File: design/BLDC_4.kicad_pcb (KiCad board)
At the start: 4 copper layers, 39.9 x 97.5 mm, 120 parts, among them J1 Conn_01x02_Pin, J101 Conn_02x16_Odd_Even, J2 Conn_01x02_Pin, J3 Conn_01x02_Pin, J4 Conn_01x02_Pin, J803 USB_C_Receptacle_USB2.0_16P, Q1 IRFS7530, Q2 IRFS7530, Q3 IRFS7530, Q4 IRFS7530, Q5 IRFS7530, Q6 IRFS7530, U1 STM32F40X_LQFP64, U2 TC2117, U3 DRV8302, U401 SN65HVD232, X2 8MHz 10ppm

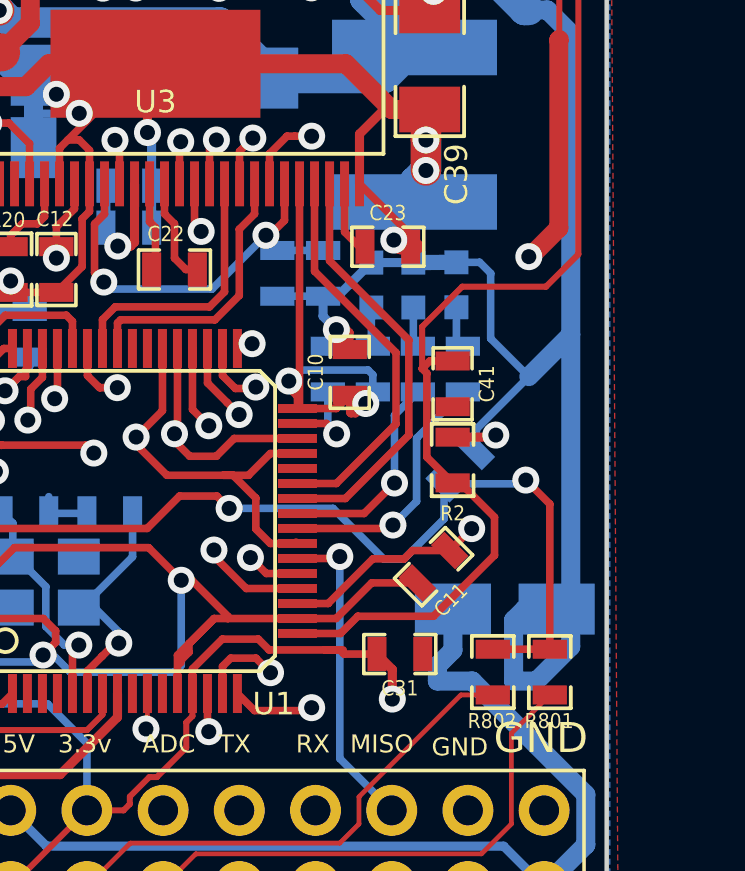
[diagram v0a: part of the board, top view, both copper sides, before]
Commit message: moved LEDs to front
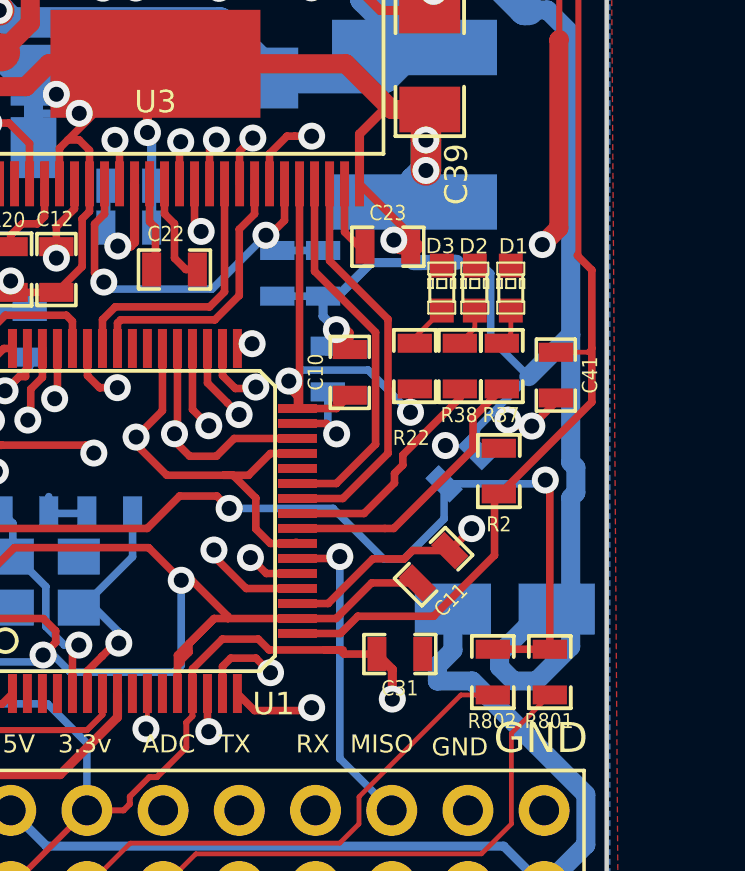
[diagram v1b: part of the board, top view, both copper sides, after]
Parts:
- D1, D2, D3, R22, R37, R38: moved to F.Cu
- moved C41 3.45 mm to (115.2, 126.2)
- moved D3 2.35 mm to (111.4, 123.3)
- moved D2 2.05 mm to (112.5, 123.3)
- moved D1 1.82 mm to (113.7, 123.3)
- moved R2 1.58 mm to (113.3, 129.4)
- moved R22 1.40 mm to (110.5, 125.9)
- moved R38 1.40 mm to (112.0, 125.9)
- moved R37 1.30 mm to (113.4, 125.9)
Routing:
- net /MCU/ADC_TEMP: track 58.0 -> 54.8 mm
- net GND: track 299.6 -> 300.5 mm, vias 29 -> 31
- net /MCU/LED_GREEN: track 8.63 -> 9.35 mm, vias 1 -> 0
- net /MCU/LED_RED: track 7.01 -> 7.69 mm, vias 1 -> 0
- net /MCU/BR_SO2: track 14.1 -> 13.4 mm
- net /MCU/BR_SO1: track 13.2 -> 12.7 mm
